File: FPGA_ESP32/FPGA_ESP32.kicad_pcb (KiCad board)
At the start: 2 copper layers, 20 x 20 mm, 41 parts, among them J1 Conn_01x18_Female, J2 CAM, J3 Conn_01x18_Female, J4 Conn_01x18_Female, U1 LFE5UM-25F-7MG285C, U10 GD25Q16CEIGR, U2 ESP32-PICO-D4, U3 TMUX1574, U4 W956D6KBKX, U6 W956D6KBKX, U7 RFX2411

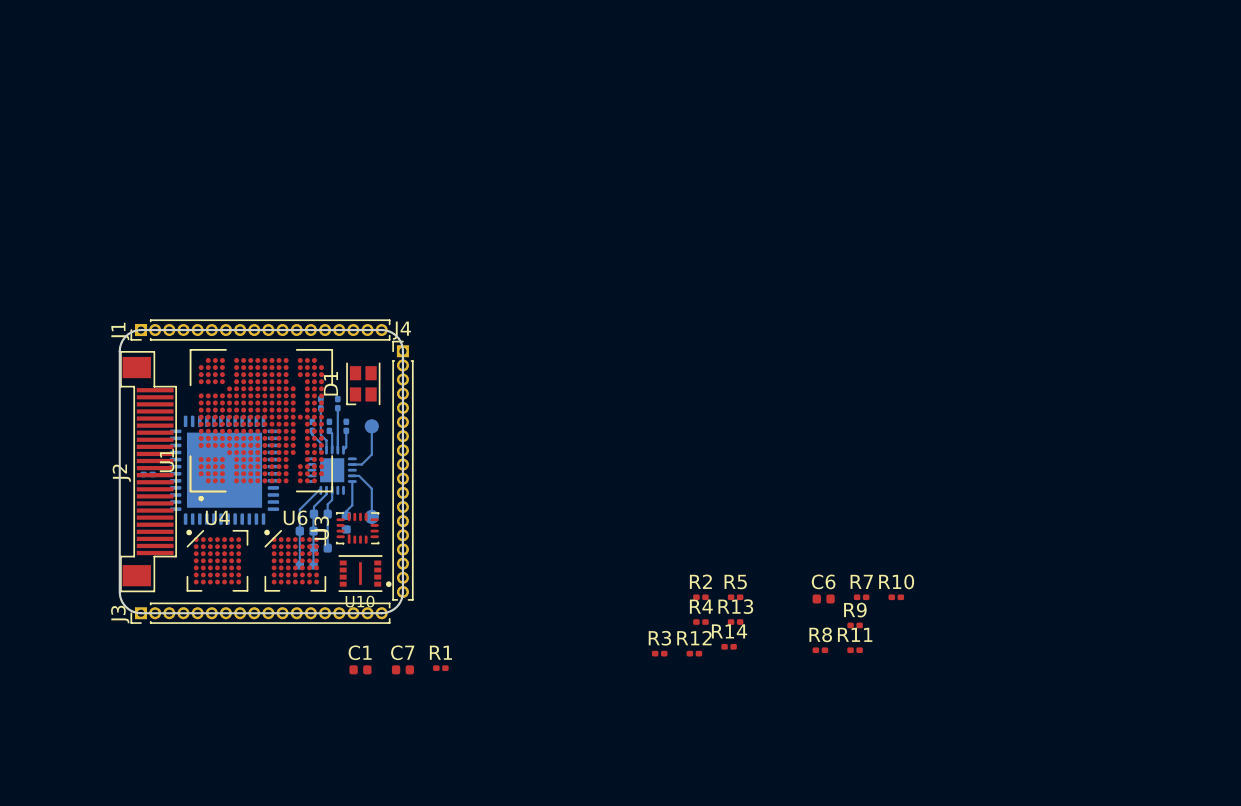
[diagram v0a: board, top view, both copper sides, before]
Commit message: FPGA_ESP32 : lot of fix + modification
Replace digital camera by analog camera decoder
Fix PSRAM io domain 3.3V -> 1.8V
Start reducing capacitor number
Add remaining psram pin
Sheet resize
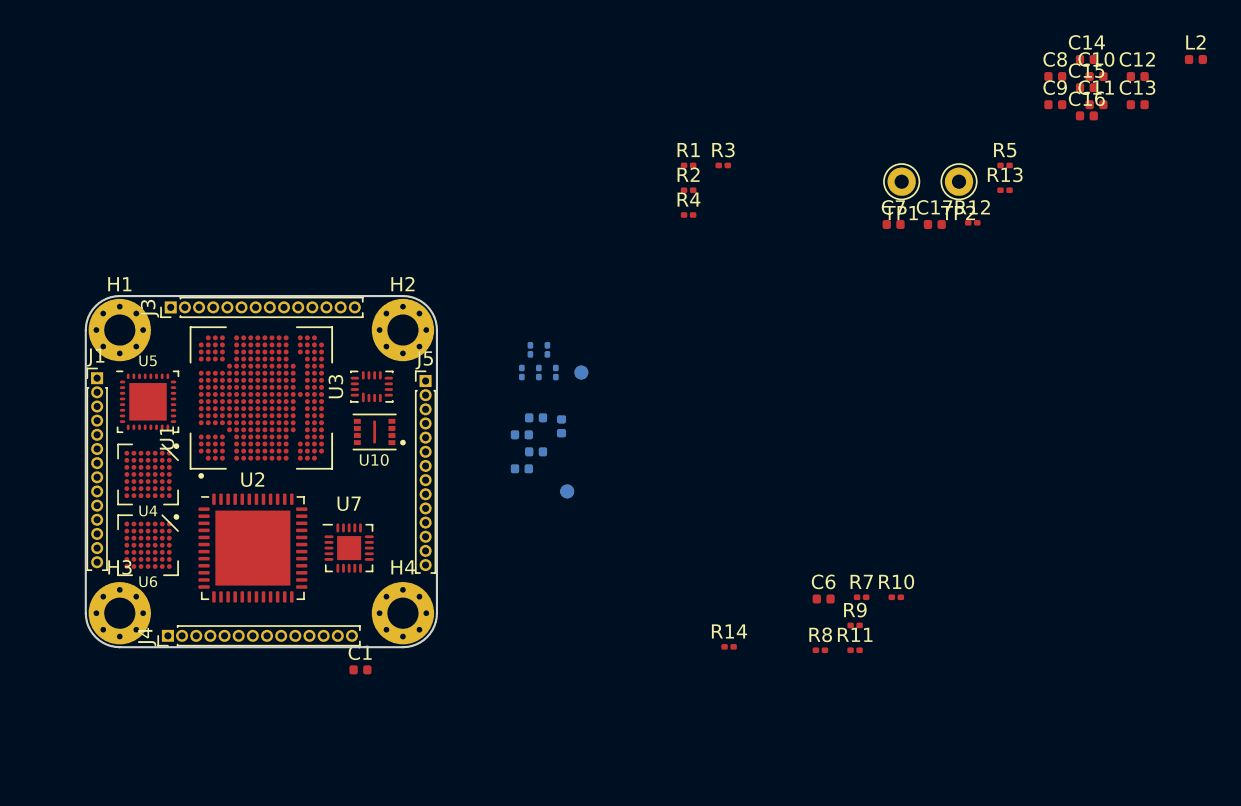
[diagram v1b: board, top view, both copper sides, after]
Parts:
- removed D1: LED_RGBC, LED_SMD:LED_Cree-PLCC4_2x2mm_CW
- removed J2: CAM, fpc_cam24:FPC_24_CAM
- removed R15: R, Resistor_SMD:R_0201_0603Metric
- added C10: 1uF, Capacitor_SMD:C_0402_1005Metric, F.Cu at (119.0, 2.10)
- added C11: 0.1uF, Capacitor_SMD:C_0402_1005Metric, F.Cu at (119.0, 4.09)
- added C12: C, Capacitor_SMD:C_0402_1005Metric, F.Cu at (121.9, 2.10)
- added C13: C, Capacitor_SMD:C_0402_1005Metric, F.Cu at (121.9, 4.09)
- added C14: 10uF, Capacitor_SMD:C_0402_1005Metric, F.Cu at (118.3, 0.90)
- added C15: 0.1uF, Capacitor_SMD:C_0402_1005Metric, F.Cu at (118.3, 2.89)
- added C16: 0.1uF, Capacitor_SMD:C_0402_1005Metric, F.Cu at (118.3, 4.88)
- added C17: C, Capacitor_SMD:C_0402_1005Metric, F.Cu at (107.6, 12.5)
- added C8: 0.1uF, Capacitor_SMD:C_0402_1005Metric, F.Cu at (116.1, 2.10)
- added C9: 0.1uF, Capacitor_SMD:C_0402_1005Metric, F.Cu at (116.1, 4.09)
- added H1: MountingHole_Pad, MountingHole:MountingHole_2.2mm_M2_Pad_Via, F.Cu at (50.0, 20.0)
- added H2: MountingHole_Pad, MountingHole:MountingHole_2.2mm_M2_Pad_Via, F.Cu at (70.0, 20.0)
- added H3: MountingHole_Pad, MountingHole:MountingHole_2.2mm_M2_Pad_Via, F.Cu at (50.0, 40.0)
- added H4: MountingHole_Pad, MountingHole:MountingHole_2.2mm_M2_Pad_Via, F.Cu at (70.0, 40.0)
- added J5: Conn_01x14_Female, Connector_PinHeader_1.00mm:PinHeader_1x14_P1.00mm_Vertical, F.Cu at (71.6, 23.6)
- added L2: L, Inductor_SMD:L_0402_1005Metric, F.Cu at (126.0, 0.90)
- added TP1: AVIN1, Connector_Pin:Pin_D1.0mm_L10.0mm, F.Cu at (105.2, 9.53)
- added TP2: AVIN2, Connector_Pin:Pin_D1.0mm_L10.0mm, F.Cu at (109.3, 9.53)
- added U5: TW9900, footprints:QFN-32_EP_4x4_Pitch0.4mm, F.Cu at (52.0, 25.1)
- C7: value 10nF -> C
- J1, J3, J4: value Conn_01x18_Female -> Conn_01x14_Female; footprint Connector_PinHeader_1.00mm:PinHeader_1x18_P1.00mm_Vertical -> Connector_PinHeader_1.00mm:PinHeader_1x14_P1.00mm_Vertical
- R1: value 1K -> 4K7
- R12, R13: value 4K7 -> 4.7K
- R5: value 4K7 -> 1M
- U2, U7: moved to F.Cu
- moved C7 46.8 mm to (104.7, 12.5)
- moved R1 39.6 mm to (90.2, 8.38)
- moved R12 36.2 mm to (110.2, 12.4)
- moved R13 35.9 mm to (112.5, 10.1)
- moved R5 35.9 mm to (112.5, 8.38)
- moved R3 34.8 mm to (92.6, 8.38)
- moved R2 28.8 mm to (90.2, 10.1)
- moved R4 28.8 mm to (90.2, 11.9)
- moved J4 26.1 mm to (53.4, 41.6), turned to 90 degrees
- moved J3 21.7 mm to (53.6, 18.4)
- moved C2 16.7 mm to (79.4, 26.2)
- moved C3 16.7 mm to (78.4, 29.8)
- moved C4 16.7 mm to (78.4, 27.4)
- moved C5 16.7 mm to (79.4, 28.6)
- moved L1 16.7 mm to (81.2, 26.8)
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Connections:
- net Net-(U2-Pad9) renamed EN
- net Net-(U3-Pad13) renamed /WIFI, BT, RT/SPI_EN
- net Net-(U3-Pad15) renamed /WIFI, BT, RT/SEL
- C7 pad 1: /FPGA/ADCREF -> Net-(C7-Pad1)
- J3 pad 10: IO23 -> IO19
- J3 pad 11: IO24 -> IO20
- J3 pad 12: IO25 -> IO21
- J3 pad 13: IO26 -> IO22
- J3 pad 14: IO27 -> IO23
- J3 pad 3: IO16 -> IO12
- J3 pad 4: IO17 -> IO13
- J3 pad 5: IO18 -> IO14
- J3 pad 6: IO19 -> IO15
- J3 pad 7: IO20 -> IO16
- J3 pad 8: IO21 -> IO17
- J3 pad 9: IO22 -> IO18
- J4 pad 1: GND -> VIO
- J4 pad 10: IO32 -> IO31
- J4 pad 11: IO33 -> IO32
- J4 pad 12: IO34 -> IO33
- J4 pad 13: IO35 -> IO34
- J4 pad 14: IO36 -> IO35
- J4 pad 2: +1V1 -> GND
- J4 pad 3: GND -> IO24
- J4 pad 4: +1V8 -> IO25
- J4 pad 5: GND -> IO26
- J4 pad 6: +2V8 -> IO27
- J4 pad 7: GND -> IO28
- J4 pad 8: VIO -> IO29
- J4 pad 9: GND -> IO30
- R1 pad 1: /FPGA/ADCREF -> VIO
- R1 pad 2: /FPGA/ADCREFOUT -> IO37
- R12 pad 1: /FPGA/CSI_I2C_SDA -> /FPGA/TW_I2C_SCK
- R12 pad 2: +1V8 -> VIO
- R13 pad 1: /FPGA/CSI_I2C_SCL -> /FPGA/TW_I2C_DAT
- R13 pad 2: +1V8 -> VIO
- R2 pad 1: VIO -> IO31
- R2 pad 2: IO37 -> VIO
- R3 pad 1: IO31 -> VIO
- R3 pad 2: VIO -> IO36
- R4 pad 1: VIO -> IO32
- R4 pad 2: IO36 -> VIO
- R5 pad 1: IO32 -> GND
- R5 pad 2: VIO -> GND
- U1 pad A12: /FPGA/CSI_Y9 -> /FPGA/VIN_CLK
- U1 pad A13: /FPGA/~CSI_RST -> /FPGA/VIN_D6
- U1 pad A15: /FPGA/CSI_VSYNC -> /FPGA/TW_I2C_DAT
- U1 pad A16: /FPGA/CSI_MCLK -> /FPGA/TW_PWRDN
- U1 pad A17: IO27 -> /FPGA/HSYNC
- U1 pad A8: Net-(U1-PadA8) -> IO30
- U1 pad A9: Net-(U1-PadA9) -> IO29
- U1 pad B12: /FPGA/CSI_Y7 -> /FPGA/VIN_D4
- U1 pad B13: /FPGA/CSI_Y2 -> /FPGA/VIN_D7
- U1 pad B15: /FPGA/CSI_HSYNC -> /FPGA/nRESET
- U1 pad B17: IO28 -> /FPGA/VSYNC
- U1 pad B18: IO29 -> /FPGA/MPOUT
- U1 pad B9: Net-(U1-PadB9) -> IO27
- U1 pad C12: /FPGA/CSI_Y8 -> /FPGA/VIN_D5
- U1 pad C13: /FPGA/CSI_Y5 -> /FPGA/VIN_D2
- U1 pad C15: /FPGA/CSI_PWDN -> /FPGA/TW_I2C_SCK
- U1 pad C16: /FPGA/CSI_PCLK -> /FPGA/TW_INT
- U1 pad C17: IO30 -> Net-(U1-PadC17)
- U1 pad C9: Net-(U1-PadC9) -> IO28
- U1 pad D13: /FPGA/CSI_Y6 -> /FPGA/VIN_D3
- U1 pad D15: /FPGA/CSI_Y4 -> /FPGA/VIN_D1
- U1 pad D16: /FPGA/CSI_Y3 -> /FPGA/VIN_D0
- U1 pad D7: VIO -> +1V8
- U1 pad G14: +1V8 -> VIO
- U1 pad H14: +1V8 -> VIO
- U1 pad J17: /FPGA/ADCREFOUT -> Net-(U1-PadJ17)
- U1 pad J2: /FPGA/ADCREF -> Net-(U1-PadJ2)
- U1 pad M1: Net-(U1-PadM1) -> IO15
- U1 pad N1: Net-(U1-PadN1) -> IO16
- U1 pad R17: IO15 -> Net-(U1-PadR17)
- U1 pad T17: IO16 -> Net-(U1-PadT17)
- U2 pad 1: Net-(U2-Pad1) -> VIO
- U2 pad 19: Net-(U2-Pad19) -> VIO
- U2 pad 3: Net-(U2-Pad3) -> VIO
- U2 pad 37: Net-(U2-Pad37) -> VIO
- U2 pad 4: Net-(U2-Pad3) -> VIO
- U2 pad 43: Net-(U2-Pad1) -> VIO
- U2 pad 46: Net-(U2-Pad1) -> VIO
- U3 pad 14: Net-(U3-Pad14) -> VIO
- U3 pad 6: Net-(U3-Pad6) -> GND
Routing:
- net VIO: track 10.2 -> 0.00 mm
- net GND: track 5.65 -> 0.00 mm
- net Net-(R17-Pad1): track 3.91 -> 0.00 mm
- net Net-(ANT1-Pad1): track 3.75 -> 0.00 mm
- net Net-(ANT2-Pad1): track 3.66 -> 0.00 mm
- net Net-(R18-Pad1): track 3.12 -> 0.00 mm
- net Net-(L1-Pad2): track 2.59 -> 0.00 mm
- net /WIFI, BT, RT/PDET: track 1.79 -> 0.00 mm
- net Net-(R19-Pad1): track 1.60 -> 0.00 mm
- net Net-(R16-Pad1): track 1.44 -> 0.00 mm
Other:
- board size 20 x 20 mm -> 24.8 x 24.8 mm

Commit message: FPGA_ESP32 : progress on power and replaced sdio by qspi
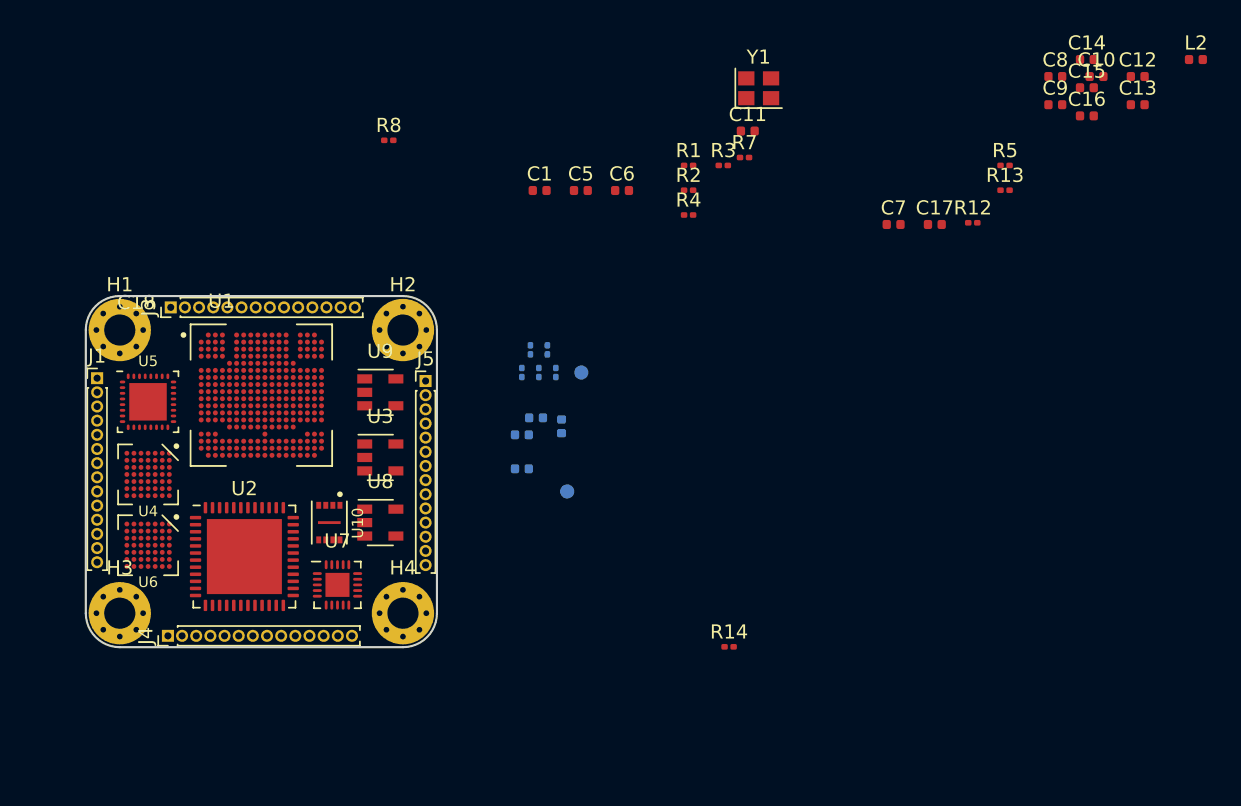
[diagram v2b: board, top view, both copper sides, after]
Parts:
- removed R10, R11, R9: 4K7, Resistor_SMD:R_0201_0603Metric
- removed TP1: AVIN1, Connector_Pin:Pin_D1.0mm_L10.0mm
- removed TP2: AVIN2, Connector_Pin:Pin_D1.0mm_L10.0mm
- added C18: 0.1uF, Capacitor_SMD:C_0402_1005Metric, F.Cu at (51.2, 19.2)
- added U8: SPX3819M5-L-1-8, Package_TO_SOT_SMD:SOT-23-5, F.Cu at (68.4, 33.6)
- added U9: SPX3819M5-L-2-5, Package_TO_SOT_SMD:SOT-23-5, F.Cu at (68.4, 24.4)
- added Y1: Crystal_GND23, Crystal:Crystal_SMD_2520-4Pin_2.5x2.0mm, F.Cu at (95.1, 2.93)
- C1, C6: value 100nF -> 10uF
- C5: value 2.2uF -> 0.1uF; moved to F.Cu
- R7: value 4K7 -> 4.7K
- R8: value 4K7 -> 10K
- U3: value TMUX1574 -> TLV71211_SOT23-5; footprint footprints:QFP-16_1.85x2.65_Pitch0.4mm -> Package_TO_SOT_SMD:SOT-23-5
- moved R8 47.2 mm to (69.0, 6.60)
- moved C1 36.1 mm to (79.7, 10.1)
- moved C6 32.2 mm to (85.5, 10.1)
- moved R7 32.1 mm to (94.1, 7.82)
- moved C11 24.7 mm to (94.4, 5.95)
- moved C5 18.7 mm to (82.6, 10.1), turned to 0 degrees
- moved U10 7.16 mm to (64.8, 33.6), turned to 270 degrees
- moved U3 5.04 mm to (68.4, 29.0), turned to 0 degrees
- moved U7 2.73 mm to (65.4, 38.0)
- moved U2 0.85 mm to (58.8, 36.0)
- moved U1 0.20 mm to (60.0, 24.6), turned to 0 degrees
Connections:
- net /WIFI, BT, RT/CS renamed /WIFI, BT, RT/SPI_FLASH_CS
- net Net-(U1-PadU17) renamed /FPGA/FPGA_HOLDN
- C1 pad 1: Net-(C1-Pad1) -> GND
- C1 pad 2: Net-(C1-Pad2) -> +1V8
- C11 pad 1: VIO -> GND
- C11 pad 2: GND -> +1V8
- C5 pad 1: VIO -> GND
- C5 pad 2: GND -> +1V8
- C6 pad 2: VIO -> +1V8
- H1 pad 1: Net-(H1-Pad1) -> GND
- H2 pad 1: Net-(H2-Pad1) -> GND
- H3 pad 1: Net-(H3-Pad1) -> GND
- H4 pad 1: Net-(H4-Pad1) -> GND
- J1 pad 1: VIO -> GND
- J1 pad 10: IO7 -> IO4
- J1 pad 11: IO8 -> IO5
- J1 pad 12: IO9 -> IO6
- J1 pad 13: IO10 -> IO7
- J1 pad 14: IO11 -> IO8
- J1 pad 2: GND -> AVIN1
- J1 pad 3: IO0 -> GND
- J1 pad 4: IO1 -> AVIN2
- J1 pad 5: IO2 -> GND
- J1 pad 6: IO3 -> IO0
- J1 pad 7: IO4 -> IO1
- J1 pad 8: IO5 -> IO2
- J1 pad 9: IO6 -> IO3
- J3 pad 10: IO19 -> IO16
- J3 pad 11: IO20 -> IO17
- J3 pad 12: IO21 -> IO18
- J3 pad 13: IO22 -> IO19
- J3 pad 14: IO23 -> IO20
- J3 pad 3: IO12 -> IO9
- J3 pad 4: IO13 -> IO10
- J3 pad 5: IO14 -> IO11
- J3 pad 6: IO15 -> IO12
- J3 pad 7: IO16 -> IO13
- J3 pad 8: IO17 -> IO14
- J3 pad 9: IO18 -> IO15
- J4 pad 10: IO31 -> IO28
- J4 pad 11: IO32 -> IO29
- J4 pad 12: IO33 -> IO30
- J4 pad 13: IO34 -> IO31
- J4 pad 14: IO35 -> IO32
- J4 pad 3: IO24 -> IO21
- J4 pad 4: IO25 -> IO22
- J4 pad 5: IO26 -> IO23
- J4 pad 6: IO27 -> IO24
- J4 pad 7: IO28 -> IO25
- J4 pad 8: IO29 -> IO26
- J4 pad 9: IO30 -> IO27
- J5 pad 10: IO36 -> /SPI_MISO
- J5 pad 11: IO37 -> IO33
- J5 pad 12: IO38 -> IO34
- J5 pad 13: IO39 -> IO35
- J5 pad 14: IO40 -> IO36
- J5 pad 2: +1V1 -> +1V8
- J5 pad 4: +1V8 -> VIO
- J5 pad 5: GND -> EN
- J5 pad 6: +2V8 -> /SPI_HD
- J5 pad 7: GND -> /SPI_WP
- J5 pad 8: VIO -> /SPI_CLK
- J5 pad 9: GND -> /SPI_MOSI
- R7 pad 1: /FPGA/SDIO1_DAT0 -> VIO
- R7 pad 2: /WIFI, BT, RT/IO2_PULL -> Net-(R7-Pad2)
- R8 pad 1: /FPGA/SDIO1_DAT1 -> VIO
- R8 pad 2: VIO -> EN
- U1 pad A10: /FPGA/SDIO1_DAT1 -> Net-(U1-PadA10)
- U1 pad A11: /FPGA/SDIO1_DAT0 -> /FPGA/VIN_CLK
- U1 pad A12: /FPGA/VIN_CLK -> /FPGA/RAM0_UB
- U1 pad A13: /FPGA/VIN_D6 -> /FPGA/RAM1_WE
- U1 pad A15: /FPGA/TW_I2C_DAT -> /FPGA/RAM0_CE
- U1 pad A16: /FPGA/TW_PWRDN -> /FPGA/RAM1_OE
- U1 pad A17: /FPGA/HSYNC -> /FPGA/RAM0_LB
- U1 pad A8: IO30 -> /FPGA/HSYNC
- U1 pad A9: IO29 -> /FPGA/TW_INT
- U1 pad B10: /FPGA/SDIO1_DAT2 -> /FPGA/VIN_D1
- U1 pad B11: /FPGA/SDIO1_CLK -> /FPGA/VIN_D5
- U1 pad B12: /FPGA/VIN_D4 -> /FPGA/RAM0_WE
- U1 pad B13: /FPGA/VIN_D7 -> /FPGA/RAM1_ADV
- U1 pad B15: /FPGA/nRESET -> /FPGA/RAM0_CLK
- U1 pad B17: /FPGA/VSYNC -> IO25
- U1 pad B18: /FPGA/MPOUT -> IO26
- U1 pad B8: Net-(U1-PadB8) -> /FPGA/TW_I2C_SCK
- U1 pad B9: IO27 -> /FPGA/nRESET
- U1 pad C10: /FPGA/SDIO1_DAT3 -> /FPGA/VIN_D0
- U1 pad C11: /FPGA/SDIO1_CMD -> /FPGA/VIN_D4
- U1 pad C12: /FPGA/VIN_D5 -> /FPGA/RAM0_ADV
- U1 pad C13: /FPGA/VIN_D2 -> /FPGA/RAM0_WAIT
- U1 pad C15: /FPGA/TW_I2C_SCK -> /FPGA/RAM1_WAIT
- U1 pad C16: /FPGA/TW_INT -> /FPGA/RAM1_CLK
- U1 pad C17: Net-(U1-PadC17) -> IO27
- U1 pad C8: Net-(U1-PadC8) -> /FPGA/TW_I2C_DAT
- U1 pad C9: IO28 -> /FPGA/TW_PWRDN
- U1 pad D13: /FPGA/VIN_D3 -> /FPGA/RAM1_CRE
- U1 pad D15: /FPGA/VIN_D1 -> /FPGA/RAM0_CRE
- U1 pad D16: /FPGA/VIN_D0 -> /FPGA/RAM0_OE
- U1 pad D7: +1V8 -> VIO
- U1 pad F1: IO21 -> IO16
- U1 pad F4: IO34 -> IO24
- U1 pad G14: VIO -> +1V8
- U1 pad G3: IO24 -> IO19
- U1 pad G4: IO38 -> IO23
- U1 pad G5: VIO -> +1V8
- U1 pad H1: IO22 -> IO17
- U1 pad H14: VIO -> +1V8
- U1 pad H18: /FPGA/RAM1_A21 -> /FPGA/RAM1_CE
- U1 pad H2: IO26 -> IO21
- U1 pad H3: IO23 -> IO18
- U1 pad H4: IO39 -> IO22
- U1 pad H5: VIO -> +1V8
- U1 pad J1: IO20 -> IO15
- U1 pad J17: Net-(U1-PadJ17) -> /FPGA/RAM1_A21
- U1 pad J2: Net-(U1-PadJ2) -> IO14
- U1 pad J3: IO25 -> IO20
- U1 pad M1: IO15 -> Net-(U1-PadM1)
- U1 pad M14: VIO -> +1V8
- U1 pad M16: Net-(U1-PadM16) -> /FPGA/RAM1_LB
- U1 pad M17: Net-(U1-PadM17) -> /FPGA/RAM1_UB
- U1 pad M18: Net-(U1-PadM18) -> /FPGA/VSYNC
- U1 pad N1: IO16 -> Net-(U1-PadN1)
- U1 pad N14: VIO -> +1V8
- U1 pad N15: Net-(U1-PadN15) -> /FPGA/VIN_D7
- U1 pad N16: Net-(U1-PadN16) -> /FPGA/VIN_D6
- U1 pad N17: Net-(U1-PadN17) -> /FPGA/MPOUT
- U1 pad N18: Net-(U1-PadN18) -> /FPGA/VIN_D3
- U1 pad N2: IO19 -> IO13
- U1 pad R16: Net-(U1-PadR16) -> /SPI_HD
- U1 pad R17: Net-(U1-PadR17) -> /FPGA/FPGA_CS
- U1 pad R18: Net-(U1-PadR18) -> /FPGA/VIN_D2
- U1 pad T17: Net-(U1-PadT17) -> /SPI_WP
- U1 pad T18: /FPGA/FLASH_MISO -> /SPI_MISO
- U1 pad U16: /WIFI, BT, RT/FLASH_CLK -> /SPI_CLK
- U1 pad U18: /FPGA/FLASH_MOSI -> /SPI_MOSI
- U1 pad V16: /FPGA/INITN -> Net-(R7-Pad2)
- U10 pad 2: Net-(U10-Pad2) -> /SPI_MISO
- U10 pad 3: /WIFI, BT, RT/WP -> /WIFI, BT, RT/HOLD
- U10 pad 5: Net-(U10-Pad5) -> /SPI_MOSI
- U10 pad 6: Net-(U10-Pad6) -> /SPI_CLK
- U10 pad 7: /FPGA/FLASH_HOLD -> /WIFI, BT, RT/WP
- U2 pad 10: IO40 -> IO29
- U2 pad 11: IO17 -> IO30
- U2 pad 17: /FPGA/SDIO1_CLK -> /FPGA/DONE
- U2 pad 18: /FPGA/SDIO1_DAT2 -> /FPGA/FPGA_CS
- U2 pad 20: /FPGA/SDIO1_DAT3 -> IO28
- U2 pad 21: /FPGA/SDIO1_CMD -> /WIFI, BT, RT/FPGA_PROGRAMN
- U2 pad 22: /FPGA/SDIO1_DAT0 -> IO33
- U2 pad 23: IO35 -> IO31
- U2 pad 24: /FPGA/SDIO1_DAT1 -> IO35
- U2 pad 34: /FPGA/INITN -> IO36
- U2 pad 35: /WIFI, BT, RT/CLK -> /SPI_CLK
- U2 pad 36: /WIFI, BT, RT/MOSI -> /SPI_MOSI
- U2 pad 38: /WIFI, BT, RT/MISO -> /SPI_MISO
- U2 pad 39: /WIFI, BT, RT/IO2_PULL -> /SPI_WP
- U2 pad 40: IO14 -> IO34
- U2 pad 41: IO13 -> IO32
- U2 pad 42: /WIFI, BT, RT/FPGA_PROGRAMN -> /SPI_HD
- U2 pad 5: IO18 -> Net-(U2-Pad5)
- U2 pad 6: /FPGA/DONE -> Net-(U2-Pad6)
- U2 pad 7: IO33 -> Net-(U2-Pad7)
- U3 pad 1: /WIFI, BT, RT/FLASH_CLK -> Net-(U3-Pad1)
- U3 pad 2: Net-(U10-Pad6) -> Net-(U3-Pad2)
- U3 pad 3: /WIFI, BT, RT/MOSI -> Net-(U3-Pad3)
- U3 pad 4: /FPGA/FLASH_MOSI -> Net-(U3-Pad4)
- U3 pad 5: Net-(U10-Pad5) -> Net-(U3-Pad5)
- U4 pad A1: Net-(U4-PadA1) -> +1V8
- U4 pad A2: Net-(U4-PadA2) -> GND
- U4 pad A3: Net-(U4-PadA3) -> +1V8
- U4 pad A4: Net-(U4-PadA4) -> GND
- U4 pad A5: Net-(U4-PadA5) -> +1V8
- U4 pad A6: Net-(U4-PadA6) -> GND
- U4 pad A7: Net-(U4-PadA7) -> +1V8
- U4 pad B1: /FPGA/RAM_WAIT -> /FPGA/RAM0_WAIT
- U4 pad B4: Net-(U4-PadB4) -> +1V8
- U4 pad C4: Net-(U4-PadC4) -> /FPGA/RAM0_OE
- U4 pad D2: Net-(U4-PadD2) -> GND
- U4 pad D6: Net-(U4-PadD6) -> GND
- U4 pad E2: Net-(U4-PadE2) -> /FPGA/RAM0_ADV
- U4 pad E3: Net-(U4-PadE3) -> GND
- U4 pad E4: Net-(U4-PadE4) -> GND
- U4 pad E5: Net-(U4-PadE5) -> GND
- U4 pad E6: Net-(U4-PadE6) -> /FPGA/RAM0_UB
- U4 pad F2: Net-(U4-PadF2) -> /FPGA/RAM0_WE
- U4 pad F4: Net-(U4-PadF4) -> /FPGA/RAM0_CRE
- U4 pad F6: Net-(U4-PadF6) -> /FPGA/RAM0_LB
- U4 pad G2: Net-(U4-PadG2) -> /FPGA/RAM0_CLK
- U4 pad G3: Net-(U4-PadG3) -> +1V8
- U4 pad G4: Net-(U4-PadG4) -> GND
- U4 pad G5: Net-(U4-PadG5) -> +1V8
- U4 pad G6: Net-(U4-PadG6) -> /FPGA/RAM0_CE
- U5 pad 2: Net-(TP2-Pad1) -> AVIN2
- U5 pad 3: Net-(TP1-Pad1) -> AVIN1
- U6 pad A1: Net-(U6-PadA1) -> +1V8
- U6 pad A2: Net-(U6-PadA2) -> GND
- U6 pad A3: Net-(U6-PadA3) -> +1V8
- U6 pad A4: Net-(U6-PadA4) -> GND
- U6 pad A5: Net-(U6-PadA5) -> +1V8
- U6 pad A6: Net-(U6-PadA6) -> GND
- U6 pad A7: Net-(U6-PadA7) -> +1V8
- U6 pad B1: /FPGA/RAM_WAIT -> /FPGA/RAM1_WAIT
- U6 pad B4: Net-(U6-PadB4) -> +1V8
- U6 pad C4: Net-(U6-PadC4) -> /FPGA/RAM1_OE
- U6 pad D2: Net-(U6-PadD2) -> GND
- U6 pad D6: Net-(U6-PadD6) -> GND
- U6 pad E2: Net-(U6-PadE2) -> /FPGA/RAM1_ADV
- U6 pad E3: Net-(U6-PadE3) -> GND
- U6 pad E4: Net-(U6-PadE4) -> GND
- U6 pad E5: Net-(U6-PadE5) -> GND
- U6 pad E6: Net-(U6-PadE6) -> /FPGA/RAM1_UB
- U6 pad F2: Net-(U6-PadF2) -> /FPGA/RAM1_WE
- U6 pad F4: Net-(U6-PadF4) -> /FPGA/RAM1_CRE
- U6 pad F6: Net-(U6-PadF6) -> /FPGA/RAM1_LB
- U6 pad G2: Net-(U6-PadG2) -> /FPGA/RAM1_CLK
- U6 pad G3: Net-(U6-PadG3) -> +1V8
- U6 pad G4: Net-(U6-PadG4) -> GND
- U6 pad G5: Net-(U6-PadG5) -> +1V8
- U6 pad G6: Net-(U6-PadG6) -> /FPGA/RAM1_CE
